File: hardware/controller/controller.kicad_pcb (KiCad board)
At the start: 2 copper layers, 100 x 100 mm, 134 parts, among them J1 230V~, J10 FAN, J11 STOP, J2 LOAD, J3 DISPLAY, J4 ENCODER, J5 TC top, J6 TC bot, J7 USB-C, J9 UART, Q1 AO3401A, Q2 BSS138, Q3 IRLML6346, Q4 IRLML6346, Q5 IRLML6346, Q6 AO3401A, Q7 IRLML6346, Q8 BSS138, SW1 RESET, SW2 BOOT, U1 IRM-10-5, U10 USBLC6-2SC6, U11 USBLC6-2SC6, U12 USBLC6-2SC6, U2 AP7361C-33E, U3 ESP32-S3-WROOM-1U-N8, U4 USBLC6-2SC6, U5 MAX31856MUD+, U6 MAX31856MUD+, U7 SN74LVC74AD, U8 TPS3828-33DBV, U9 TC6501P065

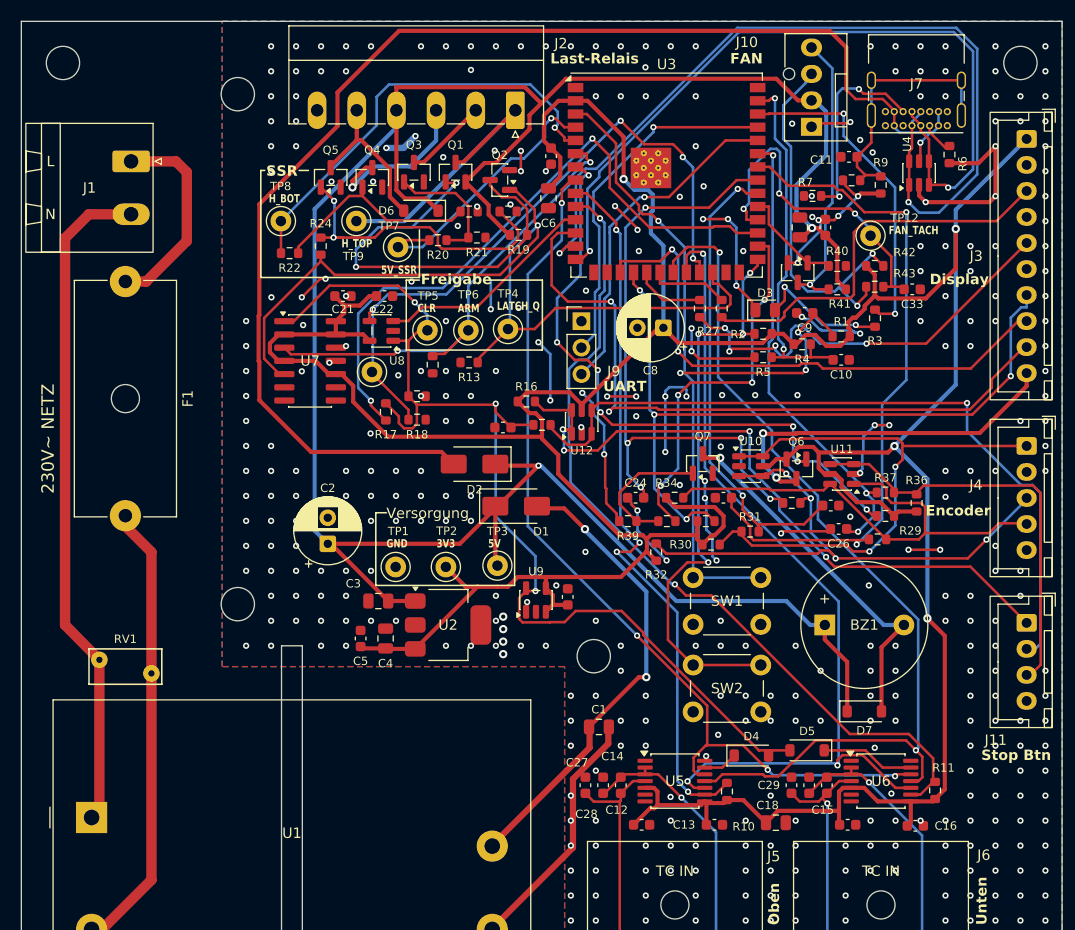
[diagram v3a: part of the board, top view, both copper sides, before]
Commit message: feat(hardware): references renumbered, fixed screw terminals J1/J2, 3D models ESP32/IRM-10
- References re-annotated by sheet position; docs, specs, firmware comment,
  check_schematic.py and DRC rule esp32_thermal_vias (U3 -> U9) updated,
  reference netlist re-exported
- Power symbols no longer excluded from simulation
- J1/J2: Phoenix MKDS 1,5/2-5,08 and MKDS 1/6-3,81 instead of pluggable
  MSTBA/MC; own footprints keep the oval pads (3 mm L-N), generated by
  make_terminal_footprints.py
- 3D models for U9 (Espressif) and U2 (Mean Well) in hardware/lib/3dmodels

Co-Authored-By: Claude Opus 5.5 <noreply@anthropic.com>
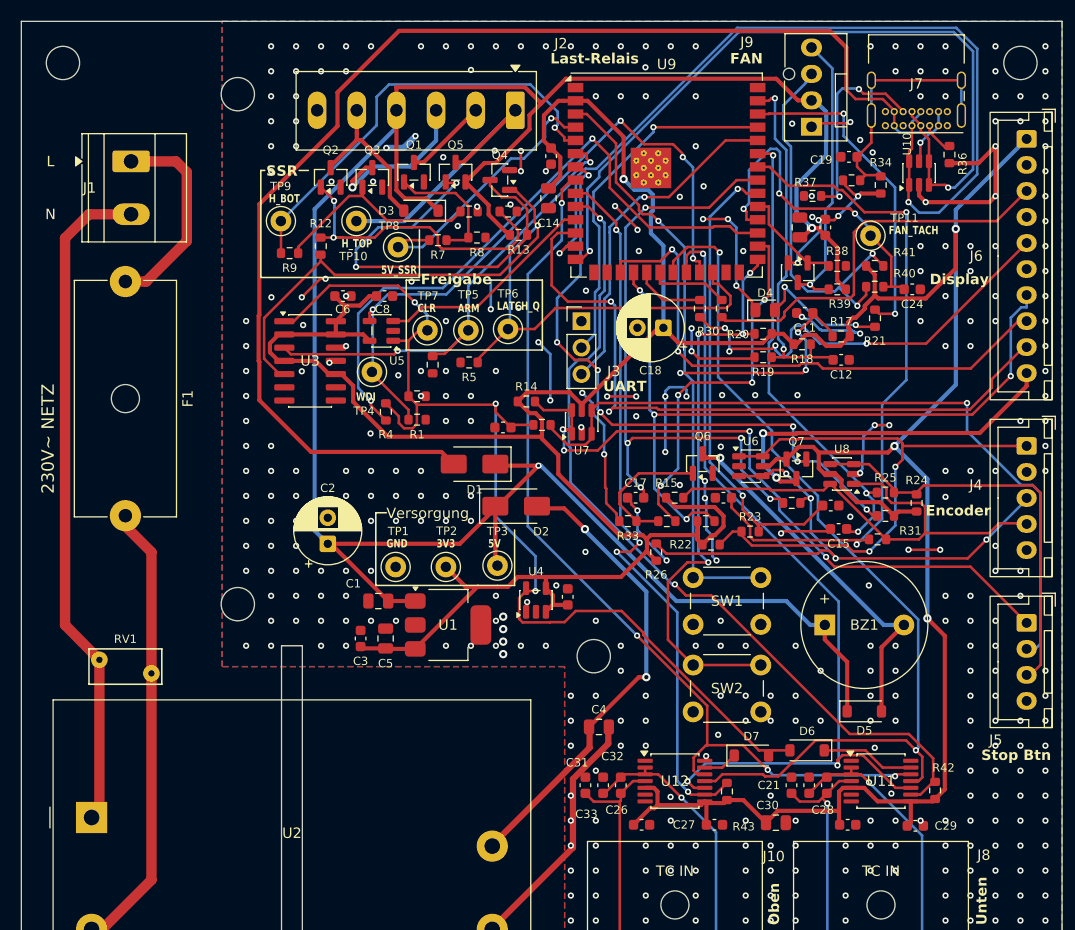
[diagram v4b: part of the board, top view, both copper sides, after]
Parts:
- J1: footprint Connector_Phoenix_MSTB:PhoenixContact_MSTBA_2,5_2-G-5,08_1x02_P5.08mm_Horizontal -> oven:Phoenix_MKDS-1,5-2-5.08_Horizontal_OvalPads
- J2: footprint Connector_Phoenix_MC:PhoenixContact_MC_1,5_6-G-3.81_1x06_P3.81mm_Horizontal -> oven:Phoenix_MKDS-1-6-3.81_Horizontal_OvalPads
- renumbered C3 to C1, C25 to C10, C9 to C11, C10 to C12, C23 to C13, C6 to C14, C26 to C15, C7 to C16, C24 to C17, C8 to C18, C11 to C19, C31 to C20, C29 to C21, C32 to C22, C17 to C23, C33 to C24, C30 to C25, C12 to C26, C13 to C27, C15 to C28, C16 to C29, C5 to C3, C18 to C30, C27 to C31, C14 to C32, C28 to C33, C1 to C4, C4 to C5, C21 to C6, C20 to C7, C22 to C8, C19 to C9, D2 to D1, D1 to D2, D6 to D3, D3 to D4, D7 to D5, D5 to D6, D4 to D7, J5 to J10, J9 to J3, J11 to J5, J3 to J6, J6 to J8, J10 to J9, Q3 to Q1, Q5 to Q2, Q4 to Q3, Q2 to Q4, Q1 to Q5, Q7 to Q6, Q6 to Q7, R18 to R1, R23 to R10, R25 to R11, R24 to R12, R19 to R13, R16 to R14, R34 to R15, R35 to R16, R1 to R17, R4 to R18, R5 to R19, R15 to R2, R2 to R20, R3 to R21, R30 to R22, R31 to R23, R36 to R24, R37 to R25, R32 to R26, R33 to R27, R26 to R29, R12 to R3, R27 to R30, R29 to R31, R38 to R32, R39 to R33, R9 to R34, R8 to R35, R6 to R36, R7 to R37, R40 to R38, R41 to R39, R17 to R4, R43 to R40, R42 to R41, R11 to R42, R10 to R43, R13 to R5, R14 to R6, R20 to R7, R21 to R8, R22 to R9, TP9 to TP10, TP12 to TP11, TP10 to TP4, TP6 to TP5, TP4 to TP6, TP5 to TP7, TP7 to TP8, TP8 to TP9, U2 to U1, U4 to U10, U6 to U11, U5 to U12, U1 to U2, U7 to U3, U9 to U4, U8 to U5, U10 to U6, U12 to U7, U11 to U8, U3 to U9
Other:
- board text added: "WDI"
